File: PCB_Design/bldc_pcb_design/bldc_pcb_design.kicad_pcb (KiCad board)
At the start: 2 copper layers, 4 parts, among them IC1 DRV8305NPHPR, U1 ESP32-WROOM-32D, U2 AS5600-ASOT, U3 LM2672M-3.3

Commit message: Annotated components and assigned footprints
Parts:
- added C1: 100 nF, Capacitor_SMD:C_0603_1608Metric, F.Cu at (212.9, 20.1)
- added C10: 1uF, Capacitor_SMD:C_0603_1608Metric, F.Cu at (212.9, 30.2)
- added C11: 0.01uF, Capacitor_SMD:C_0603_1608Metric, F.Cu at (212.9, 17.6)
- added C12: 1uF, Capacitor_SMD:C_0603_1608Metric, F.Cu at (218.0, 13.2)
- added C13: 0.01uF, Capacitor_SMD:C_0603_1608Metric, F.Cu at (222.1, 8.70)
- added C14: 4.7uF, Capacitor_SMD:C_0603_1608Metric, F.Cu at (227.3, 4.34)
- added C15: 1nF, Capacitor_SMD:C_0603_1608Metric, F.Cu at (208.9, 22.8)
- added C16: 1nF, Capacitor_SMD:C_0603_1608Metric, F.Cu at (224.9, 19.4)
- added C17: 1nF, Capacitor_SMD:C_0603_1608Metric, F.Cu at (216.9, 17.6)
- added C18: 2.2uF 16V, Capacitor_SMD:C_0603_1608Metric, F.Cu at (227.3, 6.85)
- added C19: 1uF 6.3V, Capacitor_SMD:C_0603_1608Metric, F.Cu at (222.1, 11.2)
- added C2: 68uF 10V, Capacitor_SMD:C_0603_1608Metric, F.Cu at (230.1, 14.4)
- added C20: 1uF 16V, Capacitor_SMD:C_0603_1608Metric, F.Cu at (204.9, 28.5)
- added C21: 1uF 6.3V, Capacitor_SMD:C_0603_1608Metric, F.Cu at (208.9, 25.3)
- added C22: 0.047uF, Capacitor_SMD:C_0603_1608Metric, F.Cu at (212.9, 22.6)
- added C23: 0.047uF, Capacitor_SMD:C_0603_1608Metric, F.Cu at (216.9, 20.1)
- added C24: 1uF 6.3V, Capacitor_SMD:C_0603_1608Metric, F.Cu at (208.9, 27.8)
- added C25: 2.2nF, Capacitor_SMD:C_0603_1608Metric, F.Cu at (204.9, 31.0)
- added C26: 2.2nF, Capacitor_SMD:C_0603_1608Metric, F.Cu at (222.1, 13.7)
- added C27: 2.2nF, Capacitor_SMD:C_0603_1608Metric, F.Cu at (226.1, 9.36)
- added C28: 0.1uF, Capacitor_SMD:C_0603_1608Metric, F.Cu at (220.9, 16.2)
- added C29: 0.1uF, Capacitor_SMD:C_0603_1608Metric, F.Cu at (226.1, 11.9)
- added C3: 50V 0.01uF, Capacitor_SMD:C_0603_1608Metric, F.Cu at (212.9, 32.7)
- added C4: 10 uF 50V, Capacitor_SMD:C_0603_1608Metric, F.Cu at (228.9, 16.9)
- added C5: 0.1 uF 50V, Capacitor_SMD:C_0603_1608Metric, F.Cu at (220.9, 23.8)
- added C6: 100uF 100V, Capacitor_SMD:C_0603_1608Metric, F.Cu at (216.9, 30.2)
- added C7: 1uF 50V, Capacitor_SMD:C_0603_1608Metric, F.Cu at (224.9, 21.9)
- added C8: 1uF, Capacitor_SMD:C_0603_1608Metric, F.Cu at (204.9, 26.0)
- added C9: 0.01uF, Capacitor_SMD:C_0603_1608Metric, F.Cu at (220.9, 26.3)
- added D1: 3A 40V, Diode_SMD:D_0603_1608Metric, F.Cu at (175.6, 31.5)
- added D2: LED, Diode_SMD:D_0603_1608Metric, F.Cu at (208.9, 17.6)
- added D3: LED, Diode_SMD:D_0603_1608Metric, F.Cu at (218.1, 10.7)
- added D4: LED, Diode_SMD:D_0603_1608Metric, F.Cu at (227.4, 1.79)
- added D5: LED, Diode_SMD:D_0603_1608Metric, F.Cu at (208.9, 20.2)
- added H1: MountingHole_Pad, MountingHole:MountingHole_2.7mm, F.Cu at (212.6, 12.9)
- added H2: MountingHole_Pad, MountingHole:MountingHole_2.7mm, F.Cu at (221.8, 3.97)
- added H3: MountingHole_Pad, MountingHole:MountingHole_2.7mm, F.Cu at (199.4, 28.2)
- added J1: Conn_01x04_Female, Connector_PinHeader_2.54mm:PinHeader_1x04_P2.54mm_Vertical, F.Cu at (175.9, 20.3)
- added J2: XT30PW-M, XT30PW-M:XT30PWM, F.Cu at (189.8, -10.8)
- added L1: 47uH, 8D43_Inductor:8D43, F.Cu at (194.7, 5.42)
- added R1: 10k, Resistor_SMD:R_0603_1608Metric, F.Cu at (216.9, 27.6)
- added R10: 4.7k, Resistor_SMD:R_0603_1608Metric, F.Cu at (220.9, 18.7)
- added R12: 5k, Resistor_SMD:R_0603_1608Metric, F.Cu at (212.9, 27.6)
- added R15: 330, Resistor_SMD:R_0603_1608Metric, F.Cu at (226.1, 14.4)
- added R2: 4.7k, Resistor_SMD:R_0603_1608Metric, F.Cu at (216.9, 22.6)
- added R3: 4.7k, Resistor_SMD:R_0603_1608Metric, F.Cu at (224.9, 16.9)
- added R4: 10k, Resistor_SMD:R_0603_1608Metric, F.Cu at (220.9, 21.2)
- added R5: 10k, Resistor_SMD:R_0603_1608Metric, F.Cu at (216.9, 25.1)
- added R6: 10k, Resistor_SMD:R_0603_1608Metric, F.Cu at (230.1, 11.9)
- added R7: 330, Resistor_SMD:R_0603_1608Metric, F.Cu at (212.9, 25.1)
- added R8: 100, Resistor_SMD:R_0603_1608Metric, F.Cu at (230.1, 9.36)
- added R9: 10k, Resistor_SMD:R_0603_1608Metric, F.Cu at (208.9, 30.3)
- added SW1: BOOT, Tactile_Switch:Tactile_Switch, F.Cu at (188.7, 30.5)
- added SW2: RESET, Tactile_Switch:Tactile_Switch, F.Cu at (181.7, 29.2)
- added U10: DS18S20Z+, DS18S20Z_:DS18S20Z_, F.Cu at (205.3, 3.72)
- added U4: CSD18532NQ5B, CSD18532NQ5B:CSD18532NQ5B, F.Cu at (202.7, 21.4)
- added U5: CSD18532NQ5B, CSD18532NQ5B:CSD18532NQ5B, F.Cu at (191.8, 24.8)
- added U6: CSD18532NQ5B, CSD18532NQ5B:CSD18532NQ5B, F.Cu at (214.2, 6.08)
- added U7: CSD18532NQ5B, CSD18532NQ5B:CSD18532NQ5B, F.Cu at (205.0, 12.5)
- added U8: CSD18532NQ5B, CSD18532NQ5B:CSD18532NQ5B, F.Cu at (182.9, 23.5)
- added U9: CSD18532NQ5B, CSD18532NQ5B:CSD18532NQ5B, F.Cu at (193.9, 15.9)
- IC1: footprint DRV8305NPHPR:QFP50P900X900X120-48N -> DRV8305NPHPR:DRV8305NPHPR
- U2: footprint AS5600:SOIC127P600X175-8N -> AS5600:AS5600
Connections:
- IC1 pad 14: GND -> SP1
- IC1 pad 19: SN3 -> SLC
- IC1 pad 20: SP3 -> SP1
- IC1 pad 21: SN2 -> SLB
- IC1 pad 22: SP2 -> SP1
- IC1 pad 23: SN1 -> SLA
- IC1 pad 27: SHC -> MOT_C
- IC1 pad 31: SHB -> MOT_B
- IC1 pad 35: SHA -> MOT_A
- IC1 pad 41: PVDD -> POWER_IN
- IC1 pad 45: GND -> SP1
- IC1 pad 48: DRV_VREG -> 3V3_IN
- U1 pad 1: GND -> SP1
- U1 pad 10: DRV_EN_GATE -> DRV_HC
- U1 pad 11: DRV_nFAULT -> DRV_LC
- U1 pad 12: DRV_SPI_nSCS -> DRV_EN_GATE
- U1 pad 15: GND -> SP1
- U1 pad 31: Net-(U1-Pad31) -> DRV_HA
- U1 pad 33: Net-(U1-Pad33) -> DRV_LA
- U1 pad 36: Net-(U1-Pad36) -> DRV_HB
- U1 pad 37: Net-(U1-Pad37) -> DRV_LB
- U1 pad 38: GND -> SP1
- U1 pad 39: GND -> SP1
- U1 pad 4: Net-(U1-Pad4) -> ISENB
- U1 pad 5: Net-(U1-Pad5) -> ISENC
- U1 pad 6: Net-(U1-Pad6) -> DRV_nFAULT
- U1 pad 7: Net-(U1-Pad7) -> ISENA
- U1 pad 8: Net-(U1-Pad8) -> DRV_SPI_nSCS
- U1 pad 9: Net-(U1-Pad9) -> TEMP_DQ
- U2 pad 4: GND -> SP1
- U3 pad 6: GND -> SP1

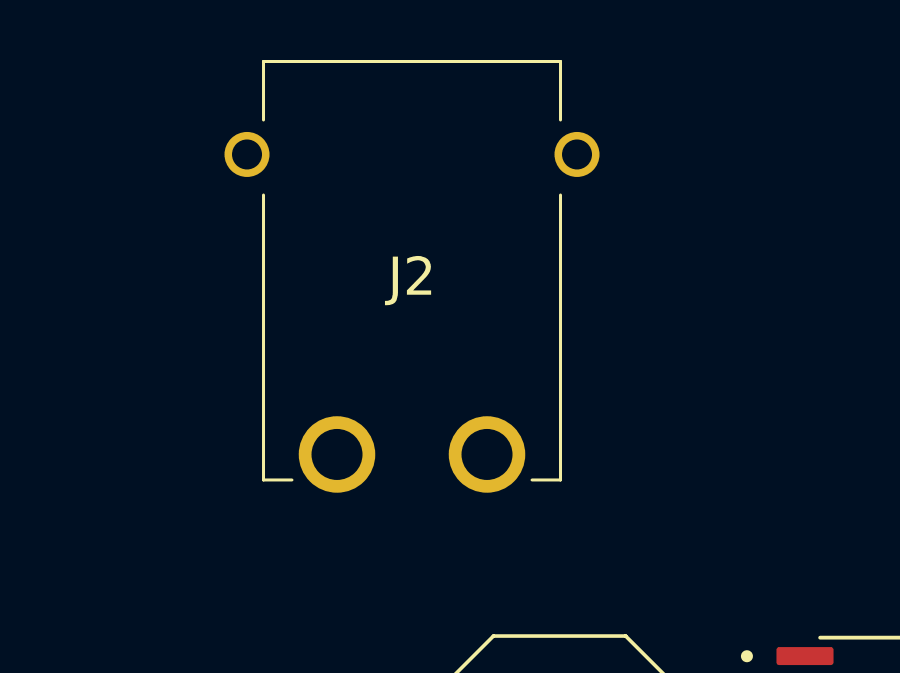
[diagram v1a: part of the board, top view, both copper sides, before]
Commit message: Replaced Xt connector with motor pads
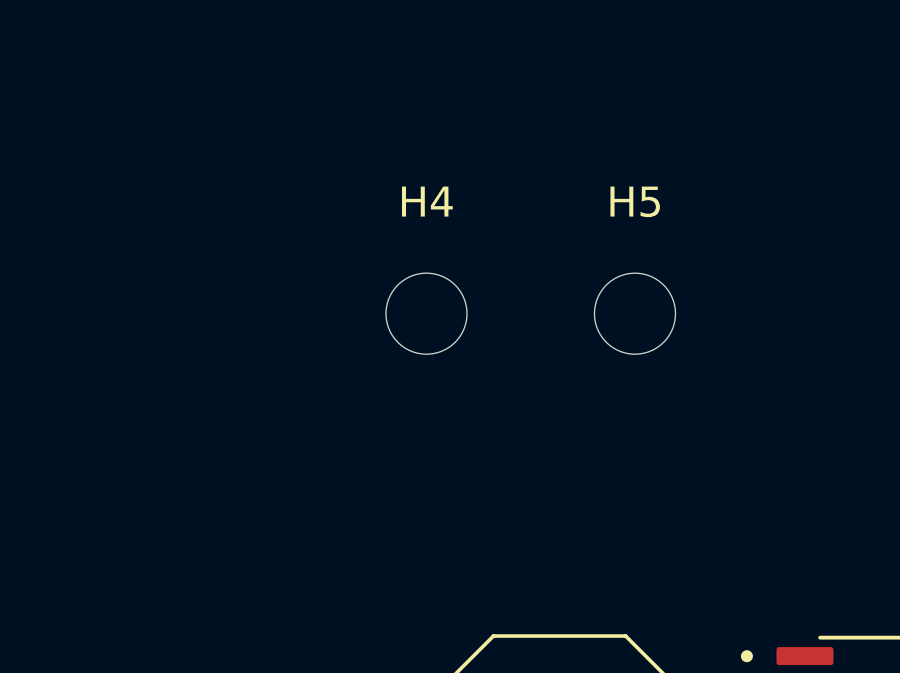
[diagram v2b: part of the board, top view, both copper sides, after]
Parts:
- removed J2: XT30PW-M, XT30PW-M:XT30PWM
- added H4: MountingHole_Pad, MountingHole:MountingHole_2.7mm, F.Cu at (190.2, -9.60)
- added H5: MountingHole_Pad, MountingHole:MountingHole_2.7mm, F.Cu at (197.2, -9.60)
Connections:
- net SP1 renamed GND

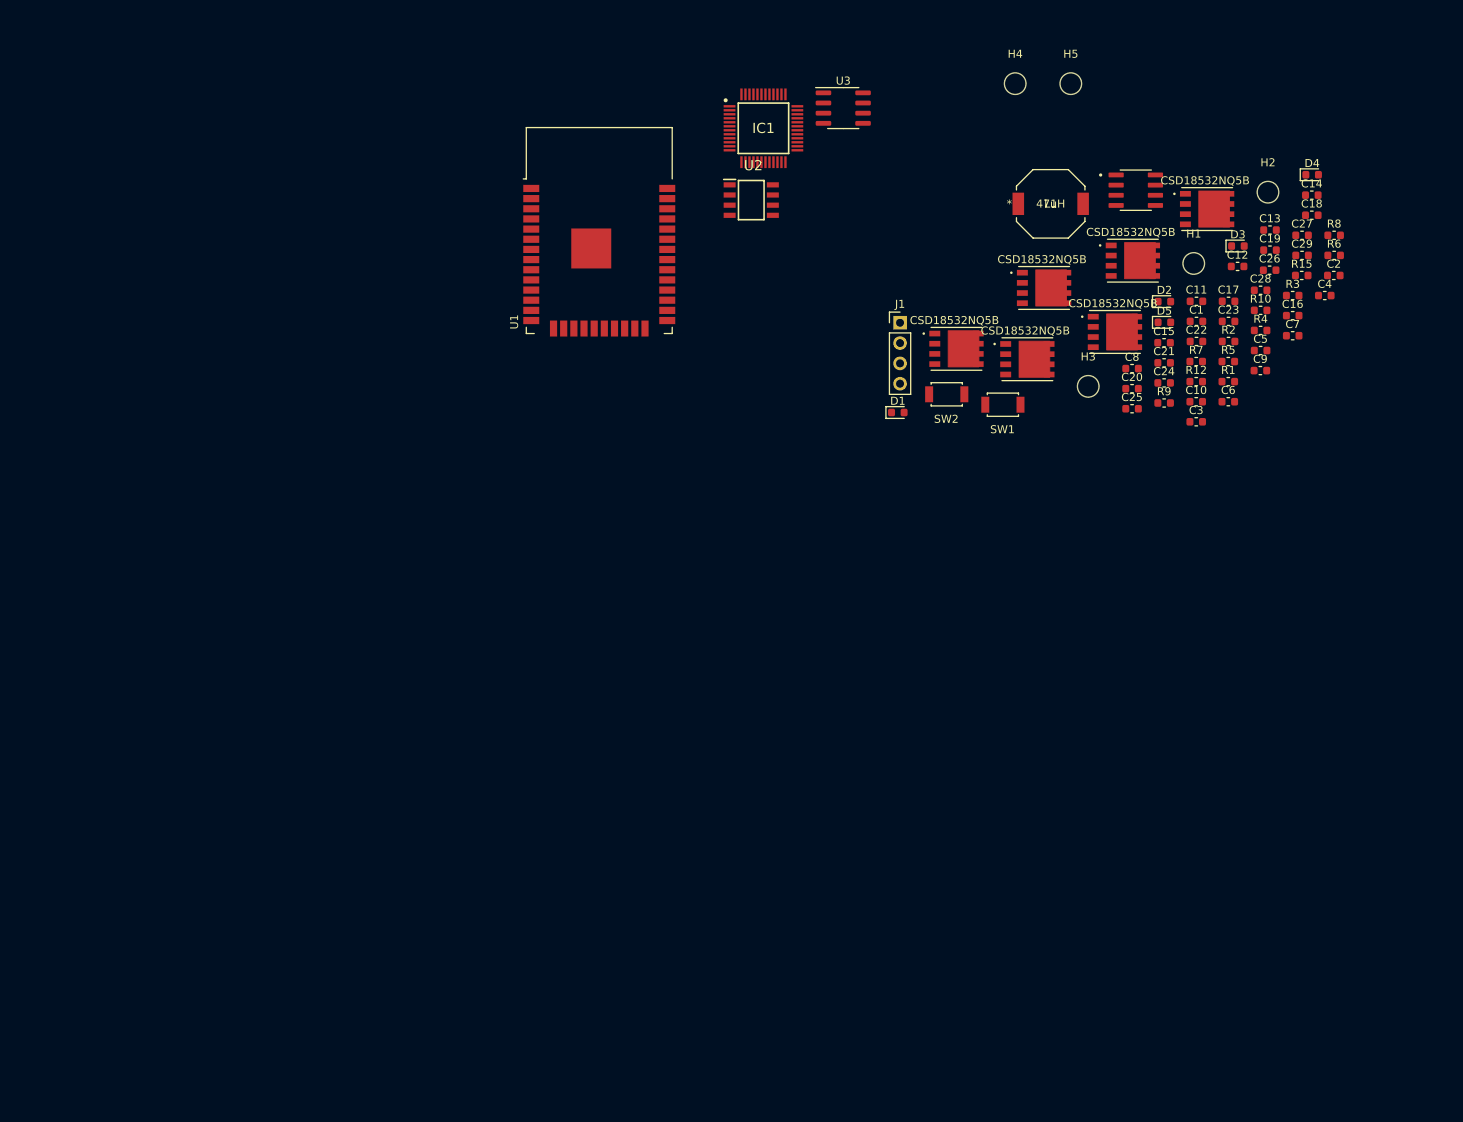
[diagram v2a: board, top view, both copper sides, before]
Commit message: Rough placement of components done for Routing. PCB Diameter : 78mm Circular
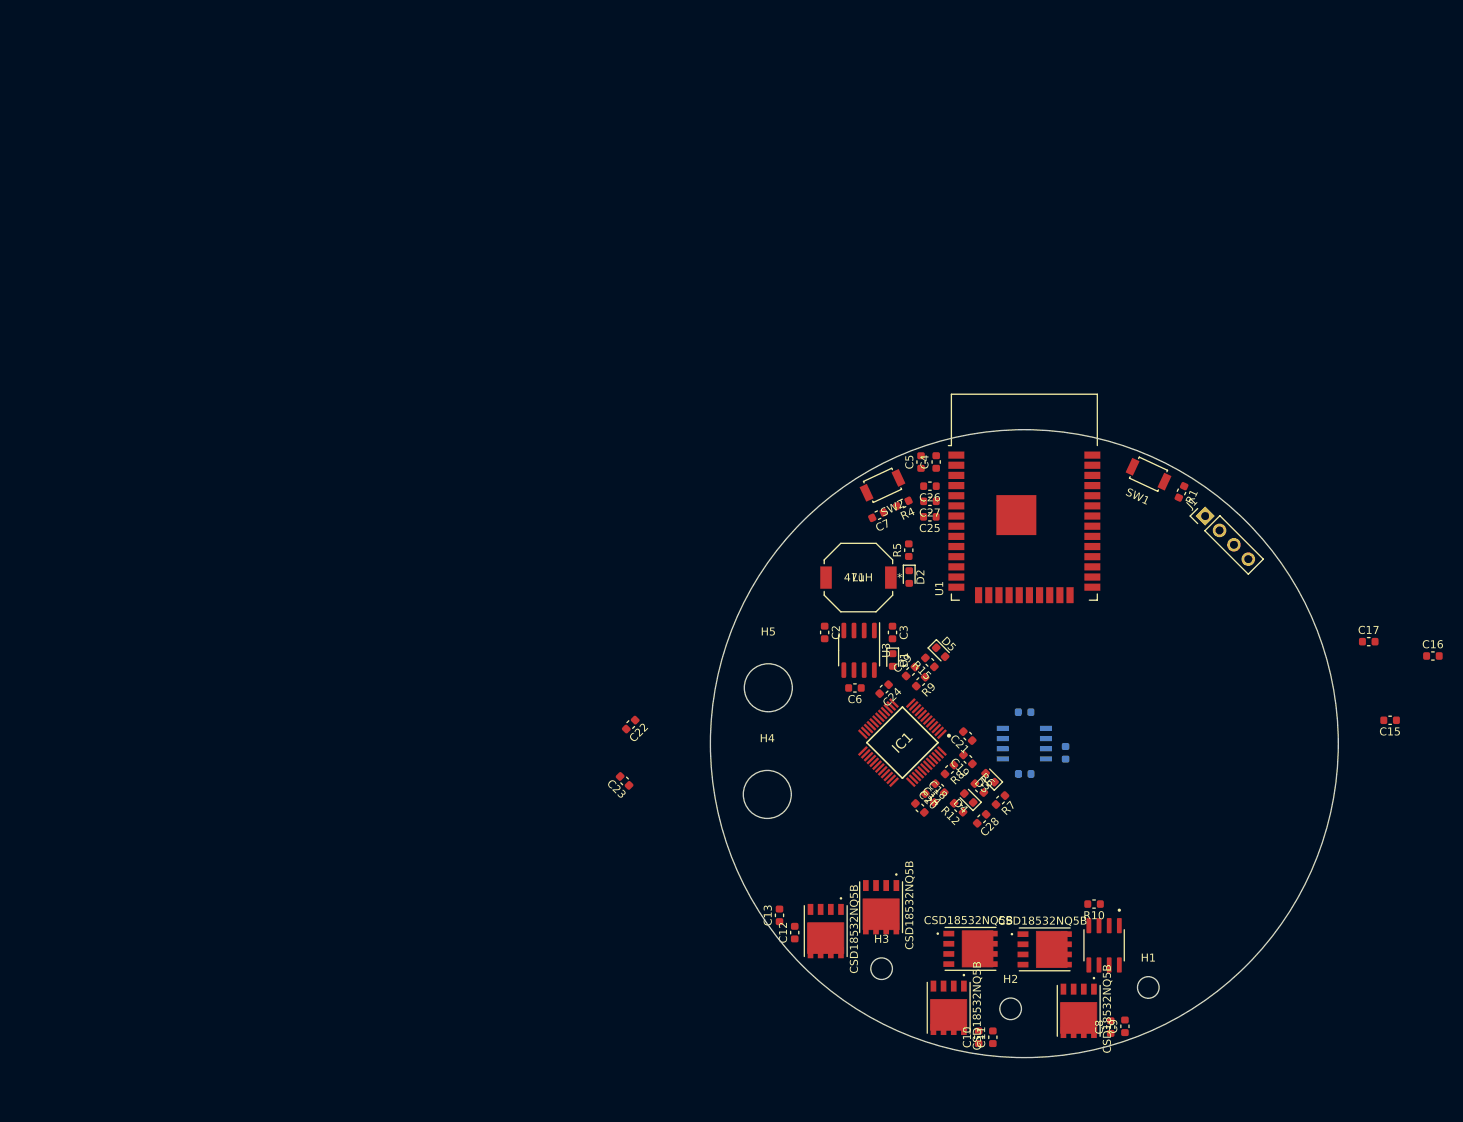
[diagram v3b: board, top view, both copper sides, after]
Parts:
- C1, R2, R3, U2: moved to B.Cu
- H4, H5: footprint MountingHole:MountingHole_2.7mm -> MountingHole:MountingHole_6mm
- moved H2 107.0 mm to (189.7, 106.0)
- moved C13 105.3 mm to (160.8, 94.4), turned to 90 degrees
- moved U6 104.9 mm to (181.9, 105.9), turned to 270 degrees
- moved C12 100.0 mm to (162.7, 96.5), turned to 90 degrees
- moved C11 95.4 mm to (187.5, 109.6), turned to 90 degrees
- moved C23 94.9 mm to (141.4, 77.6), turned to 135 degrees
- moved U10 94.5 mm to (201.4, 98.1), turned to 270 degrees
- moved H4 94.1 mm to (159.3, 79.2)
- moved H1 90.7 mm to (206.9, 103.4)
- moved D4 88.9 mm to (184.4, 79.7), turned to 135 degrees
- moved U7 88.4 mm to (184.7, 98.6)
- moved C14 87.5 mm to (180.8, 78.5), turned to 135 degrees
- moved C18 87.1 mm to (179.6, 79.7), turned to 315 degrees
- moved C22 85.4 mm to (142.2, 70.5), turned to 225 degrees
- moved U4 85.0 mm to (198.2, 106.3), turned to 270 degrees
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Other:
- board outline added: 78.5 x 78.5 mm
